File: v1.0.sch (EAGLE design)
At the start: 260 parts, among them J1 DC-044-A, J2 MICROSD-9P, J3 2p-2.54, J4 2p-2.54, J5 16p-2.54, J6 16p-2.54, J7 2x3p-2.54, J8 2p-2.54, Q2 SSM3J328R,LF, Q3 6pF@32.7680kHz, Q4 BSS138W-7-F, Q5 SSM3J328R,LF, SW1 SW-200D, SW2 SW-200D, SW3 SW-200D, SW4 SW-200D, SW5 SW-200D, SW6 SW-200D, SW7 SW-200D, SW8 SW-200D, U1 MCP23017-E/SO, U10 74HC139N, U11 BZX84C30, U12 SP483ECN-L, U13 FT232RL-SSOP28, U14 FT232RL-SSOP28, U15 FT232RL-SSOP28, U2 MCP79412-I/SN, U3 LOPY, U4 MAX213IDBR, U5 FT232RL-SSOP28, U6 FT232RL-SSOP28, U7 2x14p-2.54, U8 BR24G32-3, Y2 12MHZ

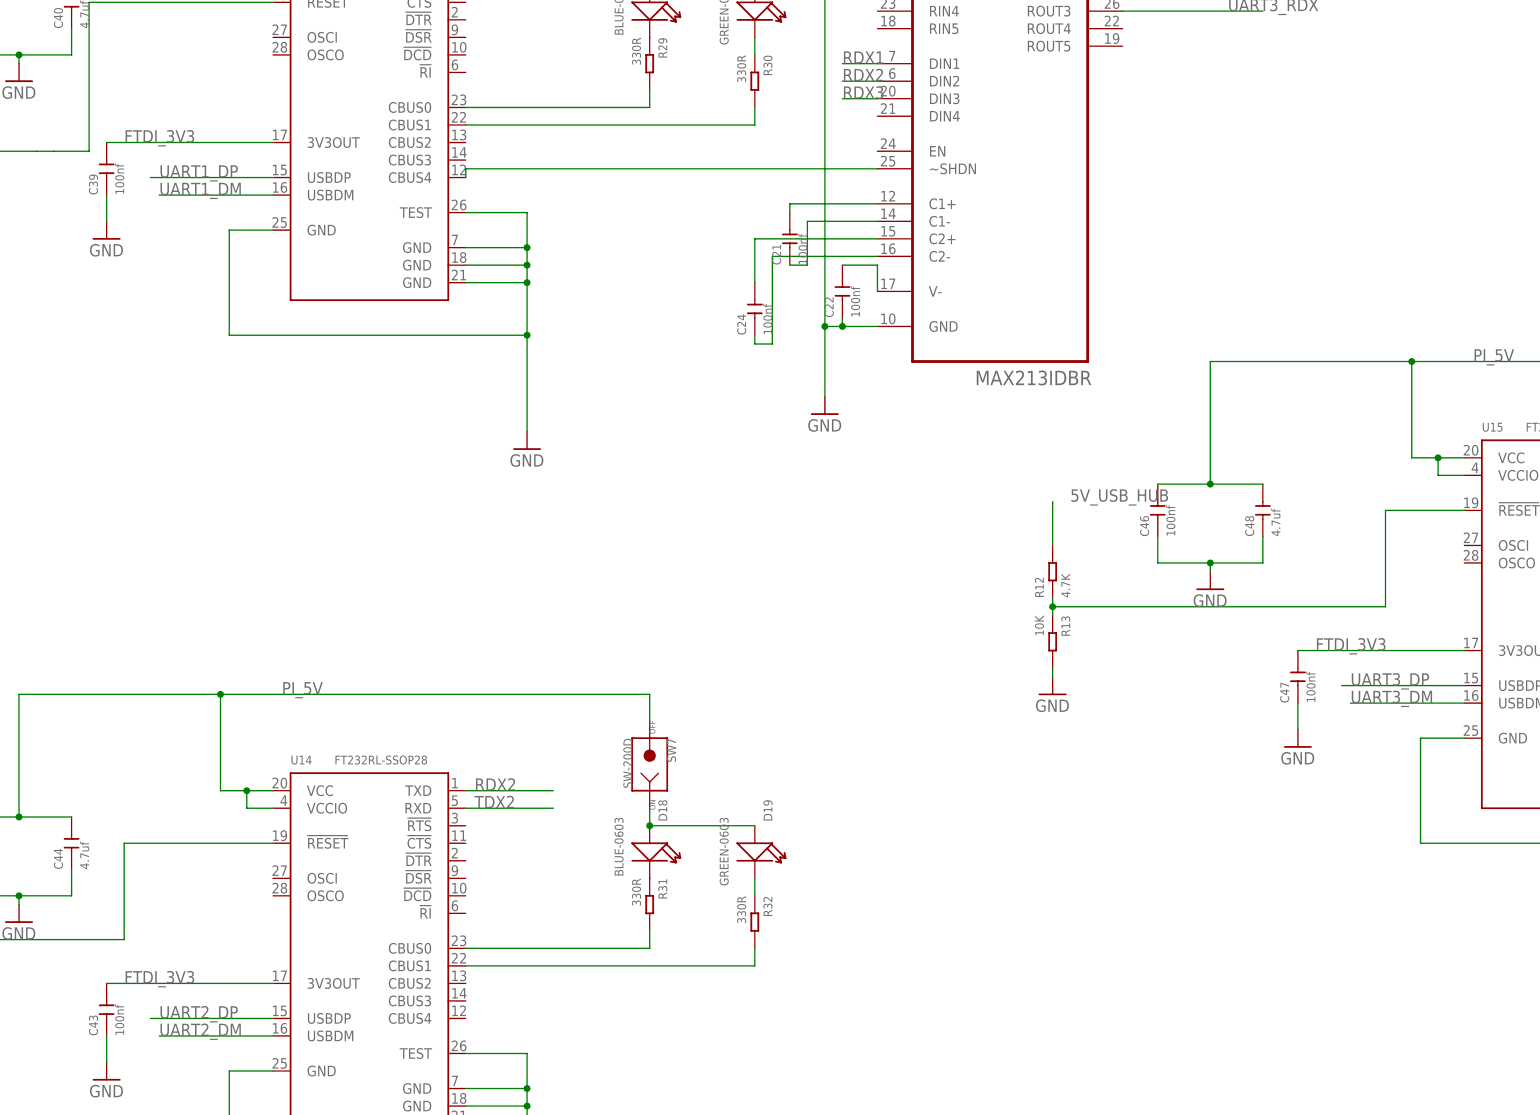
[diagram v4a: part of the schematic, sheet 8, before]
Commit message: changes names for 3v3 out for ftdi chip
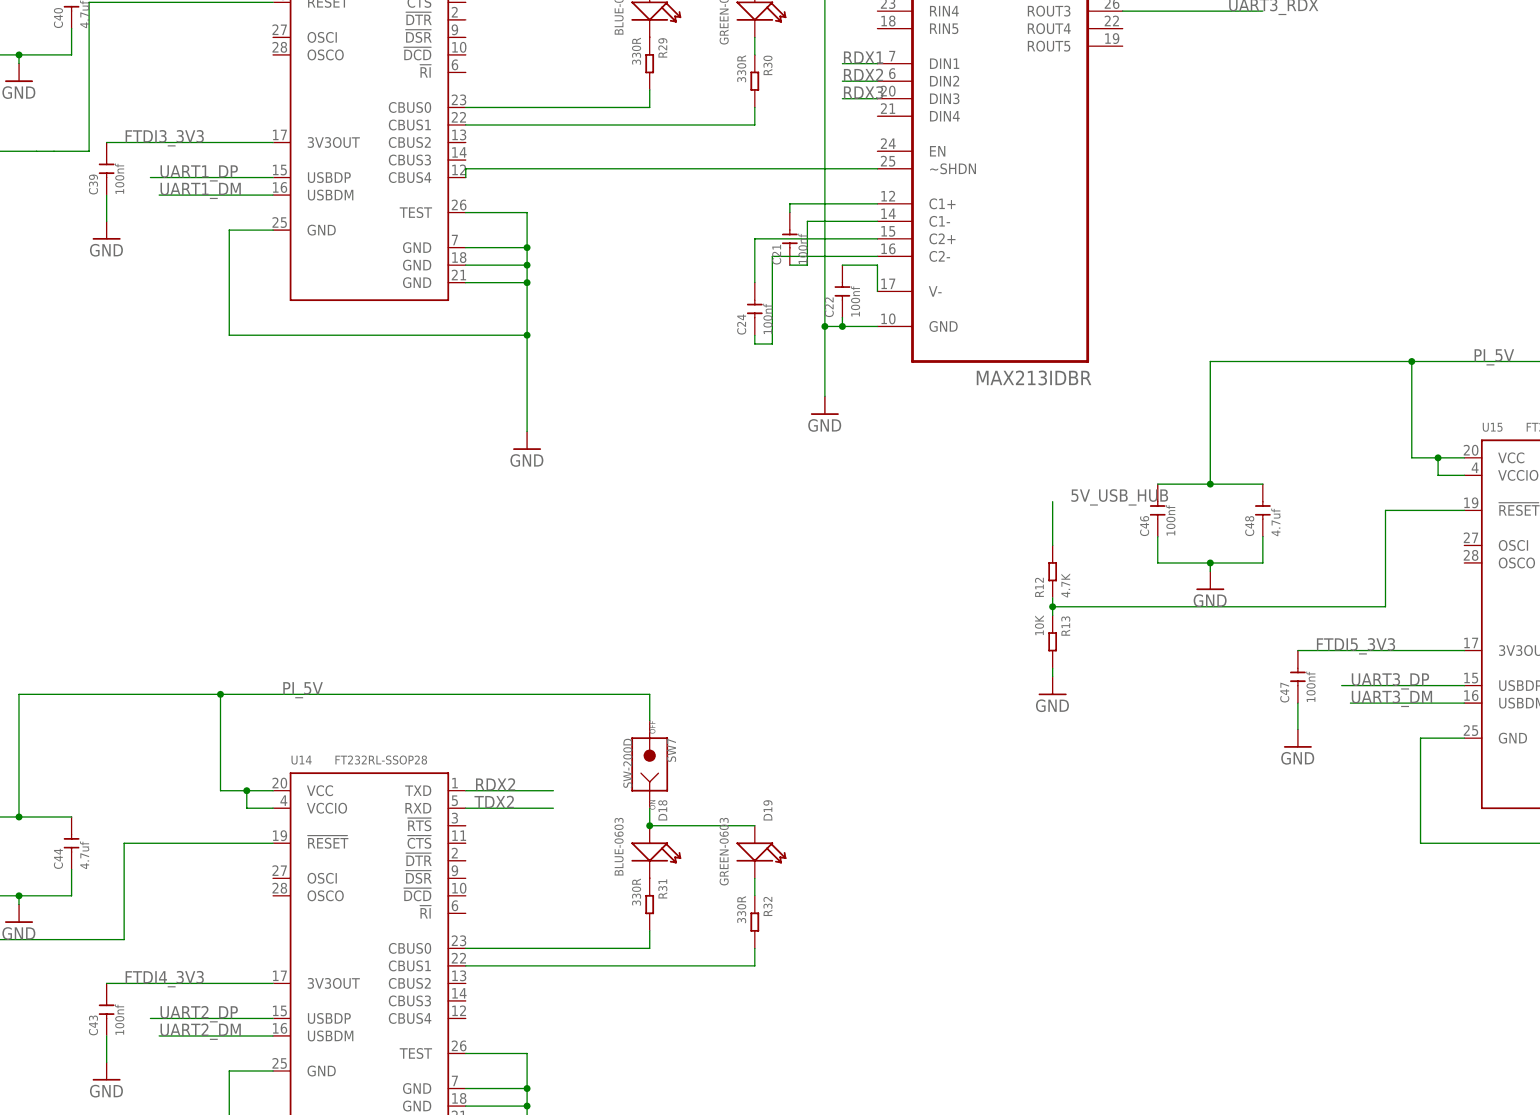
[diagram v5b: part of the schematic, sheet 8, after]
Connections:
- removed net FTDI_3V3: C39.2, C43.2, C47.2, U13.3V3OUT, U14.3V3OUT, U15.3V3OUT
- new net FTDI3_3V3: C39.2, U13.3V3OUT
- new net FTDI4_3V3: C43.2, U14.3V3OUT
- new net FTDI5_3V3: C47.2, U15.3V3OUT
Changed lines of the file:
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@@
 </segment>
 </net>
-<net name="FTDI_3V3" class="0">
-<segment>
-<pinref part="C39" gate="G$1" pin="2"/>
-<pinref part="U13" gate="1" pin="3V3OUT"/>
-<wire x1="215.9" y1="255.27" x2="240.03" y2="255.27" width="0.1524" layer="91"/>
-<label x="218.44" y="255.27" size="1.778" layer="95"/>
-</segment>
-<segment>
-<pinref part="C43" gate="G$1" pin="2"/>
-<pinref part="U14" gate="1" pin="3V3OUT"/>
-<wire x1="215.9" y1="133.35" x2="240.03" y2="133.35" width="0.1524" layer="91"/>
-<label x="218.44" y="133.35" size="1.778" layer="95"/>
-</segment>
+<net name="FTDI5_3V3" class="0">
 <segment>
 <pinref part="C47" gate="G$1" pin="2"/>
@@
 </segment>
 </net>
+<net name="FTDI3_3V3" class="0">
+<segment>
+<pinref part="C39" gate="G$1" pin="2"/>
+<pinref part="U13" gate="1" pin="3V3OUT"/>
+<wire x1="215.9" y1="255.27" x2="240.03" y2="255.27" width="0.1524" layer="91"/>
+<label x="218.44" y="255.27" size="1.778" layer="95"/>
+</segment>
+</net>
+<net name="FTDI4_3V3" class="0">
+<segment>
+<pinref part="C43" gate="G$1" pin="2"/>
+<pinref part="U14" gate="1" pin="3V3OUT"/>
+<wire x1="215.9" y1="133.35" x2="240.03" y2="133.35" width="0.1524" layer="91"/>
+<label x="218.44" y="133.35" size="1.778" layer="95"/>
+</segment>
+</net>

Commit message: fist changes
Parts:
- removed SW3, SW4: SW-200D, Seeed-Switch:DIP-TILT-SWITCH-SW-200D(2P-12X3.6MM)
- added TP10, TP11, TP12, TP9: TPB2,54, testpad:TPB2,54
- C4: device Seeed-Capacitor:CERAMIC-10UF-10V-10%-X5R(0603) -> Seeed-Capacitor:TANTALUM-SMD-10UF-10V-10%(AVX-A)
- SW1, SW2: value SW-200D -> TS-1101F; device Seeed-Switch:DIP-TILT-SWITCH-SW-200D(2P-12X3.6MM) -> Seeed-Switch:DIP-BUTTON(2P-6.0X3.0X4.3MM)-TS-1101F
- SW5, SW6, SW7, SW8: value SW-200D -> TS-1101F; device Seeed-Switch-2016:DIP-TILT-SWITCH-SW-200D(2P-12X3.6MM) -> Seeed-Switch:DIP-BUTTON(2P-6.0X3.0X4.3MM)-TS-1101F
- U$4: value MCR29300 -> MIC29300; device mic29300:MCR29300 -> mic29300:MIC29300
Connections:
- removed net N$81: D4.-, D5.-, D6.-, SW1.1
- removed net N$86: D13.-, D8.-, D9.-, SW3.1
- net 5V35: now also C4.+; no longer C4.2
- net GND: now also C4.-; no longer C4.1, SW3.2, SW4.2
- net N$122: now also TP10.TP
- net N$123: now also TP12.TP
- net N$83: now also D13.-, D4.-, D5.-, D6.-, D8.-, D9.-, SW1.1; no longer SW4.1
- net PI_5V: now also TP11.TP
- net PI_PWR_CTRL: now also TP9.TP

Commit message: all the corrections are in, I am making a another check
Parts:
- removed F57, F58: SMD1206R500SF, Seeed-Fuse:SMD-PPTC-500MA(1206)
- removed J7: 2x3p-2.54, Seeed-Connector -2016:DIP-BLACK-MALE-HEADER(2X3P-2.54）-2.54
- removed R12, R14, R4: 4.7K, Seeed-Resistor:SMD-RES-4.7K-5%-1/10W(0603)
- removed R13, R15, R8: 10K, Seeed-Resistor:SMD-RES-10K-1%-1/10W(0603)
- removed SW6, SW7, SW8: TS-1101F, Seeed-Switch:DIP-BUTTON(2P-6.0X3.0X4.3MM)-TS-1101F
- added C25: 10nf, Seeed-Capacitor-2016:CERAMIC-10NF-50V-10%-X7R(0603)
- added D12: YELLOW-WHITE-0603, Seeed-LED-2016:SMD-LED-YELLOW-WHITE(0603)
- added F60, F61, F62, F63: SMD1206R500SF, Seeed-Fuse:SMD-PPTC-500MA(1206)
- added L4: 330R-1500MA, Seeed-Inductor-2016:SMD-FERRITE-BEAD-330R-1500MA(0805)'0805'
- added R42: 330R, Seeed-Resistor-2016:SMD-RES-330R-1%-1/10W(0603)
- added SW3: TS-1101F, Seeed-Switch:DIP-BUTTON(2P-6.0X3.0X4.3MM)-TS-1101F
- added SW4: TS-1101F, Seeed-Switch-2016:DIP-BUTTON(2P-6.0X3.0X4.3MM)-TS-1101F
- added TP13, TP14, TP15: TPB2,54, testpad:TPB2,54
- added U9: 2x14p-2.54, Seeed-Connector:DIP-IC-SOCKET(2X14P-2.54)
- C30: device Seeed-Capacitor-2016:CERAMIC-4.7UF-10V-10%-X5R(0603) -> Seeed-Capacitor-2016:TANTALUM-SMD-4.7UF-16V(AVX-A)
- C34: device Seeed-Capacitor-2016:CERAMIC-10UF-25V-10%-X5R(0805) -> Seeed-Capacitor:TANTALUM-SMD-10UF-16V-10%(AVX-A)
- R25: value 4.7K -> 100R; device Seeed-Resistor:SMD-RES-4.7K-5%-1/10W(0603) -> Seeed-Resistor-2016:SMD-RES-100R-5%-1/10W(0603)
- R26: value 10K -> 22R; device Seeed-Resistor:SMD-RES-10K-1%-1/10W(0603) -> Seeed-Resistor-2016:SMD-RES-22R-5%-1/10W(0603)
- SW5: device Seeed-Switch:DIP-BUTTON(2P-6.0X3.0X4.3MM)-TS-1101F -> Seeed-Switch-2016:DIP-BUTTON(2P-6.0X3.0X4.3MM)-TS-1101F
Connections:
- net RS485_DM renamed USB1_DM
- net RS485_DP renamed USB1_DP
- net UART1_DM renamed USB2_DM
- net UART1_DP renamed USB2_DP
- net UART1_TDX renamed RS232_1_TXD
- net UART2_DP renamed USB3_DP
- net UART3_DM renamed USB4_DM
- net UART3_DP renamed USB4_DP
- net UART_RX renamed UART_RXD
- net UART_TDX renamed UART_TXD
- removed net 3V3_P: F57.2, J7.2, J7.5
- removed net FTDI2_CBUS1: R23.2, U5.CBUS0
- removed net N$100: D16.-, R29.1
- removed net N$101: D17.-, R30.1
- removed net N$107: C34.2, U$6.VD33_O
- removed net N$108: C33.2, U$6.VD18_O
- removed net N$111: D18.-, R31.1
- removed net N$112: D19.-, R32.1
- removed net N$115: D20.-, R33.1
- removed net N$116: D21.-, R34.1
- removed net N$65: D15.+, D7.+, SW5.1
- removed net N$85: D7.-, R23.1
- removed net N$92: D15.-, R24.1
- removed net N$94: D20.+, D21.+, SW6.1
- removed net N$95: D18.+, D19.+, SW7.1
- removed net N$96: D16.+, D17.+, SW8.1
- removed net N$99: R25.1, R26.1, U5.!RESET
- removed net PI_5V_PROTECTED: F58.2, J7.1, J7.6
- removed net RDX1: U13.TXD, U4.DIN1
- removed net RDX2: U14.TXD, U4.DIN2
- removed net RDX3: U15.TXD, U4.DIN3
- removed net TDX1: U13.RXD, U4.RIN1
- removed net TDX2: U14.RXD, U4.RIN2
- removed net TDX3: U15.RXD, U4.RIN3
- removed net UART1_RDX: I_UART_HUB_1-4.S, U4.ROUT1
- removed net UART2_RDX: PI_UART_HUB_2-4.S, U4.ROUT2
- removed net UART2_TDX: PI_UART_HUB_2-3.S, U4.DOUT2
- removed net UART3_RDX: PI_UART_HUB_3-4.S, U4.ROUT3
- removed net UART3_TDX: PI_UART_HUB_3-3.S, U4.DOUT3
- new net +3V3_P: F62.2, U9.26, U9.3
- new net +3V3_PP: F62.1
- new net 3V3_PPP: F63.2, U9.25, U9.4
- new net 5V_USB_HUB_FERRITE: C20.2, C23.2, C28.2, C30.+, C31.2, C38.2, C40.2, C42.2, C44.2, C46.2, C48.2, L4.2, R27.2, SW5.2, U12.VCC, U13.VCC, U13.VCCIO, U14.VCC, U14.VCCIO, U15.VCC, U15.VCCIO, U4.EN, U4.VCC, U4.~SHDN, U5.VCC, U5.VCCIO
- new net FTDI_HUB_LEDS: R23.1, R24.1, R29.1, R30.1, R31.1, R32.1, R33.1, R34.1, SW5.1
- new net GPIO16_FREE: PCB1.GPIO16, U9.24, U9.5
- new net GPIO18_FREE: U9.23, U9.6
- new net GPIO19_FREE: PCB1.GPIO19, U9.22, U9.7
- new net GPIO20_FREE: PCB1.GPIO20, U9.21, U9.8
- new net GPIO21_FREE: PCB1.GPIO21, U9.20, U9.9
- new net GPIO24_FREE: PCB1.GPIO24, U9.11, U9.18
- new net GPIO25_FREE: PCB1.GPIO25, U9.12, U9.17
- new net GPIO26_FREE: PCB1.GPIO26, U9.13, U9.16
- new net N$10: D7.-, U5.CBUS0
- new net N$42: D7.+, R23.2
- new net N$43: R42.2, TP15.TP, U$6.DRV
- new net N$44: TP13.TP, U$6.LED1
- new net N$45: TP14.TP, U$6.LED2
- new net N$47: R25.2, R26.1
- new net N$48: R25.1, SW3.2
- new net N$49: D12.+, R42.1
- new net N$50: D12.-, SW4.2
- new net N$51: D21.+, R34.2
- new net N$52: D16.+, R29.2
- new net N$53: D17.+, R30.2
- new net N$55: D18.+, R31.2
- new net N$56: D19.+, R32.2
- new net PI_5V_PP: F61.2, U9.2, U9.27
- new net PI_5V_PROT: F60.2, U9.1, U9.28
- new net RS232_1_RXD: I_UART_HUB_1-4.S, U4.RIN1
- new net RS232_2_RXD: PI_UART_HUB_2-4.S, U4.RIN2
- new net RS232_2_TDX: PI_UART_HUB_2-3.S
- new net RS232_2_TXD: U4.DOUT2
- new net RS232_3_RXD: PI_UART_HUB_3-4.S, U4.RIN3
- new net RS232_3_TDX: PI_UART_HUB_3-3.S
- new net RS232_3_TXD: U4.DOUT3
- new net RXD1: U13.RXD, U4.DIN1
- new net RXD2: U14.RXD, U4.DIN2
- new net RXD3: U15.RXD, U4.DIN3
- new net SHIELD: C25.1, C9.1, USB1.GND, USB1.SHIELD, USB3.GND, USB3.SHIELD
- new net TXD1: U13.TXD, U4.ROUT1
- new net TXD2: U14.TXD, U4.ROUT2
- new net TXD3: U15.TXD, U4.ROUT3
- new net USB3_DM: U$6.DM3
- net +3V3: now also F10.1, F12.1, F14.1, F16.1, F18.1, F20.1, F22.1, F23.1, F25.1, F27.1, F29.1, F3.1, F31.1, F33.1, F35.1, F37.1, F47.1, F49.1, F51.1, F53.1, F55.1, F6.1, F63.1, F8.1; no longer F57.1
- net 3V3_SMOOTH: no longer F10.1, F12.1, F14.1, F16.1, F18.1, F20.1, F22.1, F23.1, F25.1, F27.1, F29.1, F3.1, F31.1, F33.1, F35.1, F37.1, F47.1, F49.1, F51.1, F53.1, F55.1, F6.1, F8.1
- net 5V_USB_HUB: now also C25.2; no longer R12.2, R14.2, R25.2, R4.2
- net FTID2_CBUS2: now also D15.-; no longer R24.2
- net GND: now also C22.2, C30.-, C34.-, SW4.1, U9.10, U9.14, U9.19; no longer C22.1, C30.1, C34.1, C9.1, J7.3, J7.4, R13.2, R15.2, R26.2, R8.2, USB1.GND, USB3.GND
- net N$105: now also C33.2, U$6.VD18_O
- net N$106: now also C34.+, U$6.VD33_O
- net N$109: now also D16.-; no longer R29.2
- net N$110: now also D17.-; no longer R30.2
- net N$113: now also D18.-; no longer R31.2
- net N$114: now also D19.-; no longer R32.2
- net N$117: now also D20.-; no longer R33.2
- net N$118: now also D21.-; no longer R34.2
- net N$17: now also C22.1, U4.V-; no longer C21.2, U4.C1+
- net N$23: now also C21.1, U4.C1+; no longer R12.1, R13.1, U15.!RESET
- net N$25: now also C21.2; no longer C21.1
- net N$28: now also D20.+, R33.2; no longer C22.2, U4.V-
- net N$31: now also D15.+, R24.2; no longer R14.1, R15.1, U14.!RESET
- net N$4: no longer U4.~SHDN
- net N$5: no longer R4.1, R8.1
- net PI_5V: now also F60.1, F61.1; no longer C20.2, C23.2, C28.2, C30.2, C31.2, C38.2, C40.2, C42.2, C44.2, C46.2, C48.2, F58.1, R27.2, SW5.2, SW6.2, SW7.2, SW8.2, U12.VCC, U13.VCC, U13.VCCIO, U14.VCC, U14.VCCIO, U15.VCC, U15.VCCIO, U4.VCC, U5.VCC, U5.VCCIO
- net RS485_A: now also SW3.1
- net RS485_B: now also R26.2
- net UART2_DM: no longer U$6.DM3
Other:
- note added: "Added new header with free rpi gpio and 5V, 3V3 and GND"
- note added: "DHT22"
- note added: "FREE RPI GPIOs"
- note added: "Seed does not have 120R resistors, so put a 100R and 22R resistors in series."
- note removed: "disable for these LEDS?"
- moved on the sheet: C21, C22, C24, C42, C43, C44, D15, D16, D17, D18, D19, D20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

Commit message: added corrections and had a check
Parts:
- C40, C44, C48: value 4.7uf -> 47uf; device Seeed-Capacitor-2016:CERAMIC-4.7UF-10V-10%-X5R(0603) -> Seeed-Capacitor-2016:TANTALUM-SMD-47UF-6.3V(AVX-A)
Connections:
- net LOPY_RX0 renamed LOPY_RXD0
- net LOPY_RX1 renamed LOPY_RXD1
- net LOPY_TX0 renamed LOPY_TXD0
- net LOPY_TX1 renamed LOPY_TXD1
- net N$44 renamed USB_HUB_LED1
- net N$45 renamed USB_HUB_LED2
- net UART_RXD renamed PI_TTL_RXD
- net UART_TXD renamed PI_TTL_TXD
- removed net N$4: U13.CBUS4
- removed net N$5: U13.!RESET
- removed net RS232_2_TDX: PI_UART_HUB_2-3.S
- removed net RS232_3_TDX: PI_UART_HUB_3-3.S
- removed net UART2_DM: U14.USBDM
- net 5V_USB_HUB: now also L4.1
- net 5V_USB_HUB_FERRITE: now also C40.+, C44.+, C48.+; no longer C40.2, C44.2, C48.2
- net GND: now also C40.-, C44.-, C48.-; no longer C40.1, C44.1, C48.1
- net RS232_2_TXD: now also PI_UART_HUB_2-3.S
- net RS232_3_TXD: now also PI_UART_HUB_3-3.S
- net SPI_GPIO2: now also U10.1A1
- net SPI_GPIO4: no longer U10.1A1
- net USB3_DM: now also U14.USBDM
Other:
- note added: "Address 1101111"
- note added: "Is shield really connected to GND?"
- note removed: "Seed crystals have the wrong capacitance"
- moved on the sheet: C29, TP13, TP14
